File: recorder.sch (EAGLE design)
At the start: 46 parts, among them M1 ELECTRET_MICROPHON-WM-61A, Q1 4.096MHz, T1 MMBT3904 NPN, U1 ISD15100

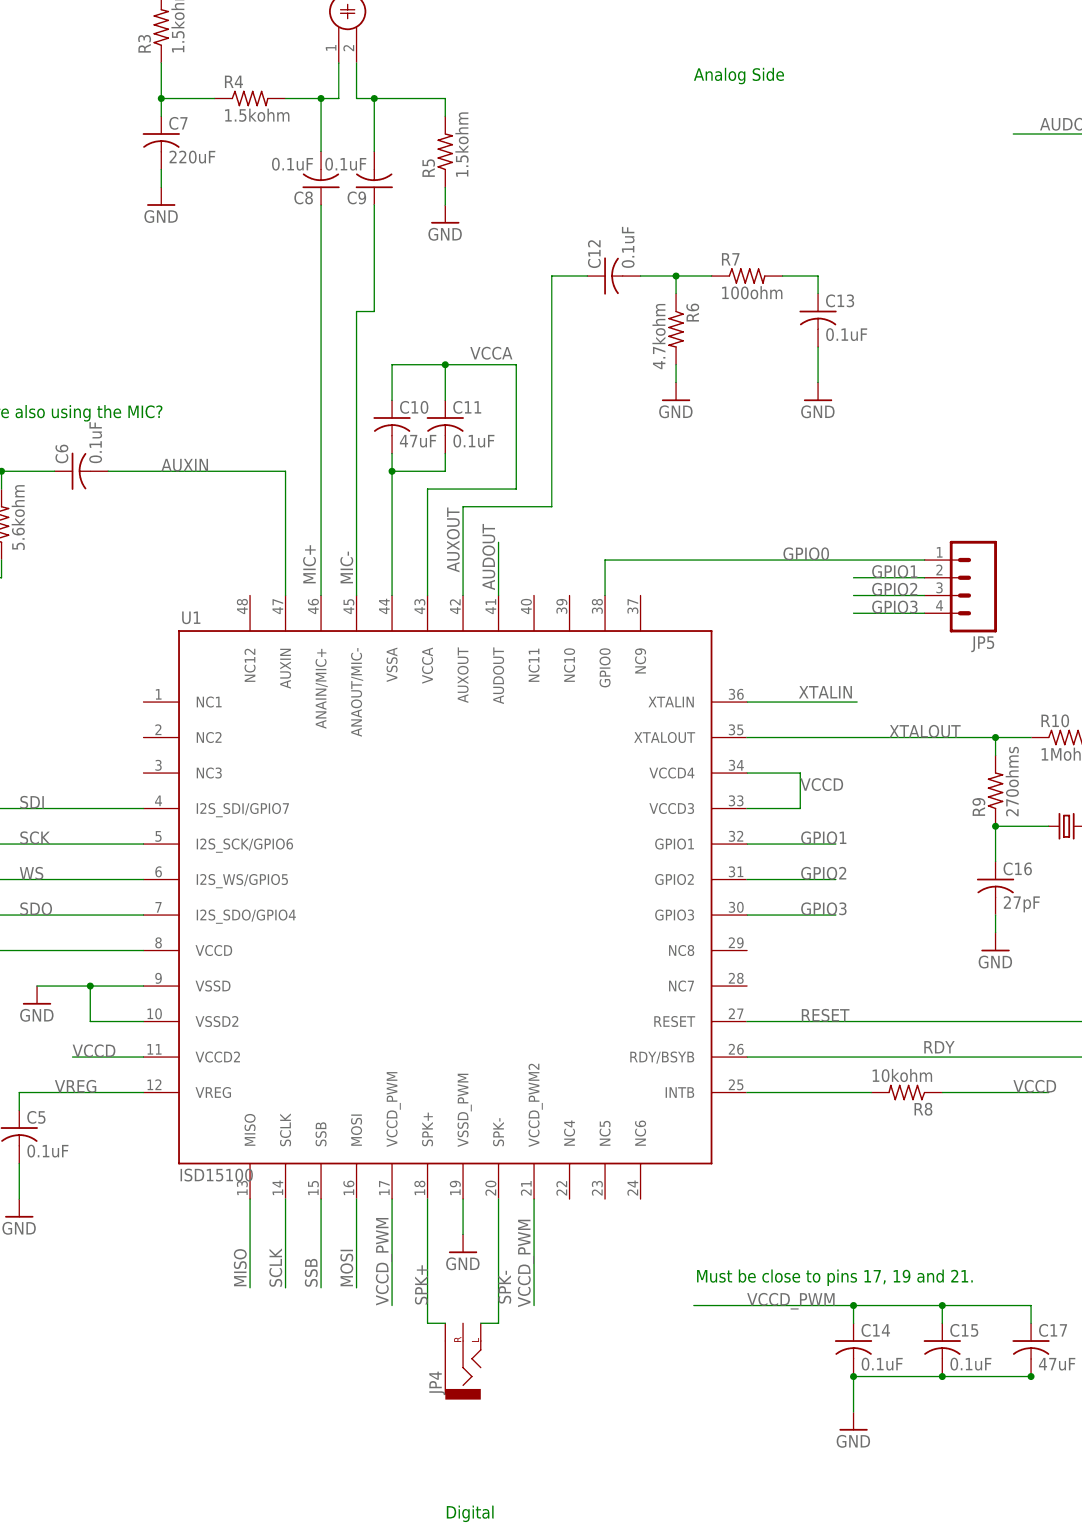
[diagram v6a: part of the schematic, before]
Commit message: upodated BOM. changed mic, headphone jack, and other passive components
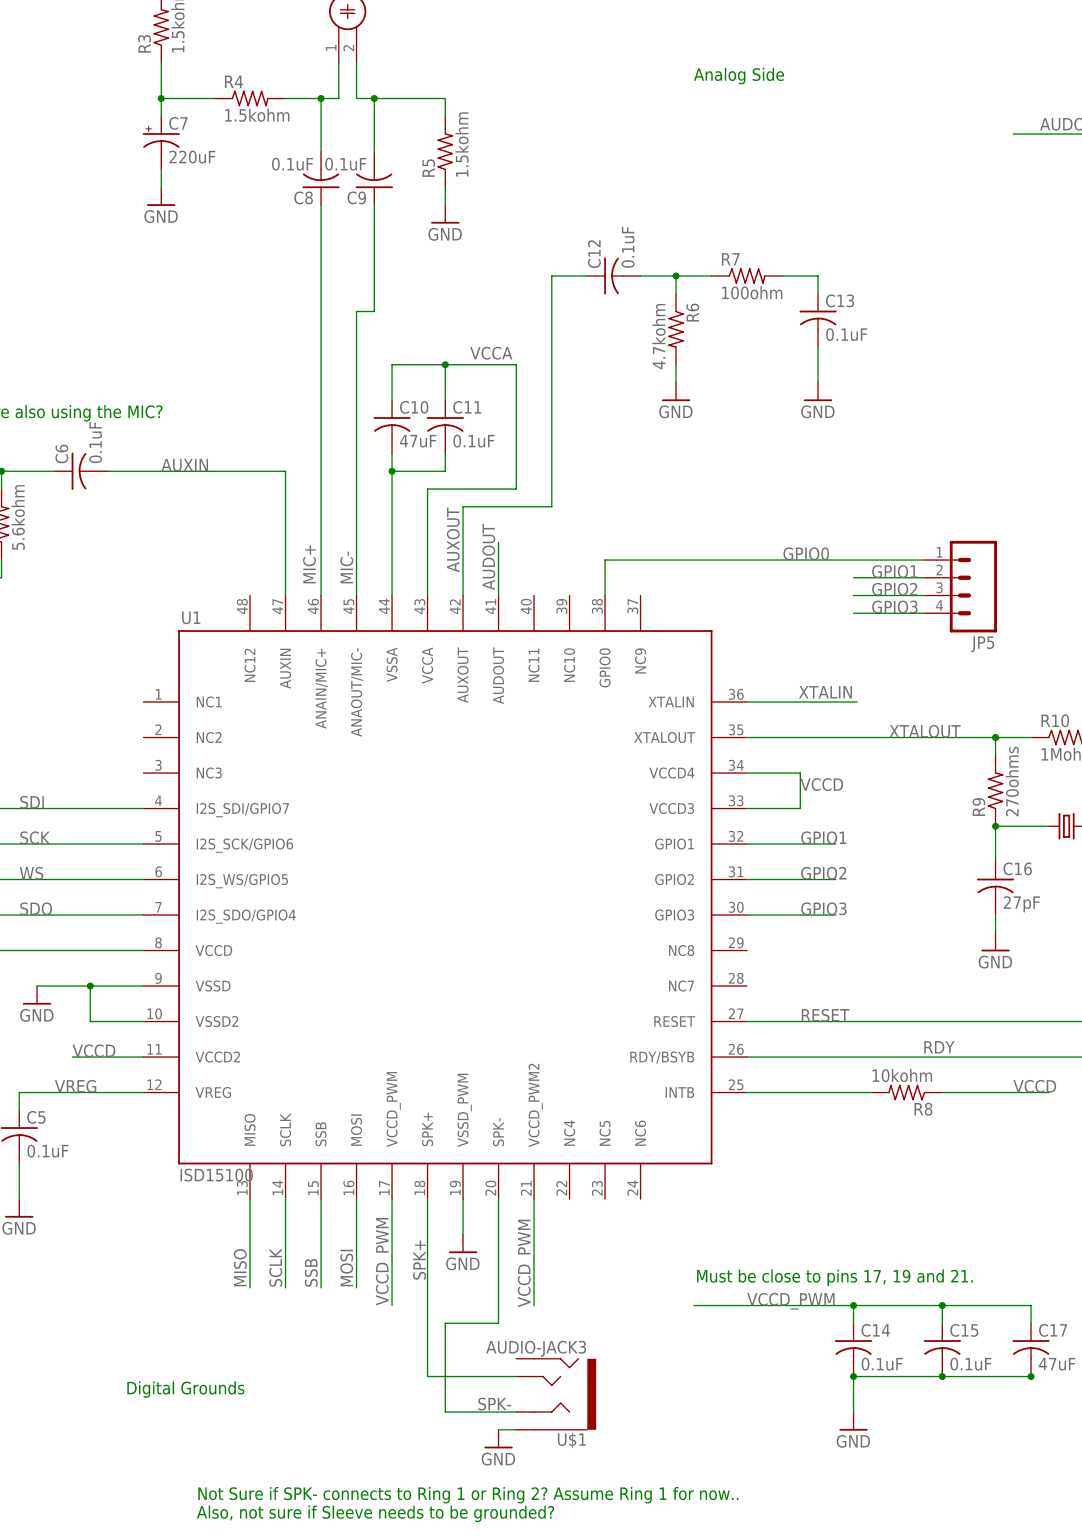
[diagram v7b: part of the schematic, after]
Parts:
- removed JP4: (no value), SparkFun-Connectors:AUDIO-JACKSMD2
- added U$1: AUDIO-JACK3, SparkFun-Connectors:AUDIO-JACK3
- C7: device rcl:C-USC0402 -> rcl:CPOL-US175TMP-0808
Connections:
- net GND: now also C7.-, U$1.EARTH; no longer C7.2
- net N$28: now also C7.+; no longer C7.1
- net SPK+: now also U$1.TIP; no longer JP4.SLEEVE
- net SPK-: now also U$1.RING1; no longer JP4.LEFT
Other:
- note added: "Digital Grounds"
- note added: "Not Sure if SPK- connects to Ring 1 or Ring 2? Assume Ring 1 for now.. Also, not sure if Sleeve needs to be grounded?"
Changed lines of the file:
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@@
 <attribute name="OC_NEWARK" value="81C8514"/>
 </part>
-<part name="C7" library="rcl" deviceset="C-US" device="C0402" value="220uF"/>
 <part name="R3" library="rcl" deviceset="R-US_" device="R0201" value="1.5kohm">
 <attribute name="MF" value="AVX CORPORATION"/>
@@
 <part name="R14" library="rcl" deviceset="R-US_" device="R0402" value="80.6kohm"/>
 <part name="Q1" library="adafruit" deviceset="CRYSTAL" device="SM49" value="4.096MHz"/>
-<part name="JP4" library="SparkFun-Connectors" deviceset="AUDIO-JACK" device="SMD2"/>
 <part name="JP5" library="SparkFun-Connectors" deviceset="M04" device="PTH"/>
 <part name="JP2" library="SparkFun-Connectors" deviceset="M04" device="PTH"/>
@@
 <part name="JP8" library="SparkFun-Connectors" deviceset="M02" device="PTH"/>
 <part name="C1" library="rcl" deviceset="C-US" device="C1206" value="47uF"/>
+<part name="U$1" library="SparkFun-Connectors" deviceset="AUDIO-JACK3" device=""/>
+<part name="GND18" library="SparkFun-Aesthetics" deviceset="GND" device=""/>
+<part name="C7" library="rcl" deviceset="CPOL-US" device="175TMP-0808" value="220uF"/>
 </parts>
 <sheets>
@@
 <text x="106.68" y="223.52" size="1.778" layer="91">Is this redundant if we have a headphone jack? Should speaker be off-board or mounted to PCB?</text>
 <text x="-121.92" y="86.36" size="1.778" layer="91">Digital Side</text>
-<text x="30.48" y="-7.62" size="1.778" layer="91">Digital</text>
+<text x="-15.24" y="10.16" size="1.778" layer="91">Digital Grounds</text>
 <text x="193.04" y="88.9" size="1.778" layer="91">Digital</text>
 <text x="66.04" y="198.12" size="1.778" layer="91">Analog Side</text>
+<text x="-5.08" y="-7.62" size="1.778" layer="91">Not Sure if SPK- connects to Ring 1 or Ring 2? Assume Ring 1 for now..
+Also, not sure if Sleeve needs to be grounded?</text>
 </plain>
 <instances>
@@
 <attribute name="MPN" x="2.54" y="195.58" size="1.778" layer="96" rot="R90" display="off"/>
 </instance>
-<instance part="C7" gate="G$1" x="-10.16" y="190.5"/>
 <instance part="R3" gate="G$1" x="-10.16" y="205.74" rot="R90">
 <attribute name="OC_NEWARK" x="-10.16" y="205.74" size="1.778" layer="96" rot="R180" display="off"/>
@@
 <instance part="R14" gate="G$1" x="149.86" y="81.28" rot="R270"/>
 <instance part="Q1" gate="G$1" x="119.38" y="91.44"/>
-<instance part="JP4" gate="G$1" x="33.02" y="15.24" rot="R90"/>
 <instance part="JP5" gate="G$1" x="104.14" y="127" rot="R180"/>
 <instance part="JP2" gate="G$1" x="-68.58" y="12.7"/>
@@
 <instance part="JP8" gate="G$1" x="-91.44" y="71.12"/>
 <instance part="C1" gate="G$1" x="-66.04" y="68.58"/>
+<instance part="U$1" gate="G$1" x="45.72" y="10.16" rot="R180"/>
+<instance part="GND18" gate="1" x="38.1" y="2.54"/>
+<instance part="C7" gate="G$1" x="-10.16" y="190.5"/>
 </instances>
 <busses>
@@
 <segment>
 <pinref part="U1" gate="G$1" pin="SPK+"/>
-<wire x1="27.94" y1="20.32" x2="27.94" y2="38.1" width="0.1524" layer="91"/>
-<wire x1="30.48" y1="20.32" x2="27.94" y2="20.32" width="0.1524" layer="91"/>
-<pinref part="JP4" gate="G$1" pin="SLEEVE"/>
-<label x="27.94" y="22.86" size="1.778" layer="95" rot="R90"/>
+<wire x1="27.94" y1="12.7" x2="27.94" y2="38.1" width="0.1524" layer="91"/>
+<label x="27.686" y="26.416" size="1.778" layer="95" rot="R90"/>
+<pinref part="U$1" gate="G$1" pin="TIP"/>
+<wire x1="27.94" y1="12.7" x2="40.64" y2="12.7" width="0.1524" layer="91"/>
 </segment>
 </net>
@@
 <pinref part="U1" gate="G$1" pin="SPK-"/>
 <wire x1="38.1" y1="20.32" x2="38.1" y2="38.1" width="0.1524" layer="91"/>
-<wire x1="35.56" y1="20.32" x2="38.1" y2="20.32" width="0.1524" layer="91"/>
-<pinref part="JP4" gate="G$1" pin="LEFT"/>
-<label x="38.1" y="27.94" size="1.778" layer="95" rot="R270"/>
+<label x="35.052" y="7.874" size="1.778" layer="95"/>
+<wire x1="38.1" y1="20.32" x2="30.48" y2="20.32" width="0.1524" layer="91"/>
+<wire x1="30.48" y1="20.32" x2="30.48" y2="7.62" width="0.1524" layer="91"/>
+<pinref part="U$1" gate="G$1" pin="RING1"/>
+<wire x1="30.48" y1="7.62" x2="40.64" y2="7.62" width="0.1524" layer="91"/>
 </segment>
 </net>
@@
 <net name="N$28" class="0">
 <segment>
-<pinref part="C7" gate="G$1" pin="1"/>
 <pinref part="R3" gate="G$1" pin="1"/>
 <wire x1="-10.16" y1="193.04" x2="-10.16" y2="195.58" width="0.1524" layer="91"/>
@@
 <wire x1="-2.54" y1="195.58" x2="-10.16" y2="195.58" width="0.1524" layer="91"/>
 <junction x="-10.16" y="195.58"/>
+<pinref part="C7" gate="G$1" pin="+"/>
 </segment>
 </net>
@@
 </segment>
 <segment>
-<pinref part="C7" gate="G$1" pin="2"/>
 <wire x1="-10.16" y1="182.88" x2="-10.16" y2="185.42" width="0.1524" layer="91"/>
 <pinref part="GND2" gate="1" pin="GND"/>
+<pinref part="C7" gate="G$1" pin="-"/>
 </segment>
 <segment>
@@
 <wire x1="-78.74" y1="71.12" x2="-78.74" y2="66.04" width="0.1524" layer="91"/>
 </segment>
+<segment>
+<pinref part="GND18" gate="1" pin="GND"/>
+<pinref part="U$1" gate="G$1" pin="EARTH"/>
+<wire x1="38.1" y1="5.08" x2="40.64" y2="5.08" width="0.1524" layer="91"/>
+</segment>
 </net>
 </nets>
@@
 </schematic>
 </drawing>
+<compatibility>
+<note version="6.3" minversion="6.2.2" severity="warning">
+Since Version 6.2.2 text objects can contain more than one line,
+which will not be processed correctly with this version.
+</note>
+</compatibility>
 </eagle>

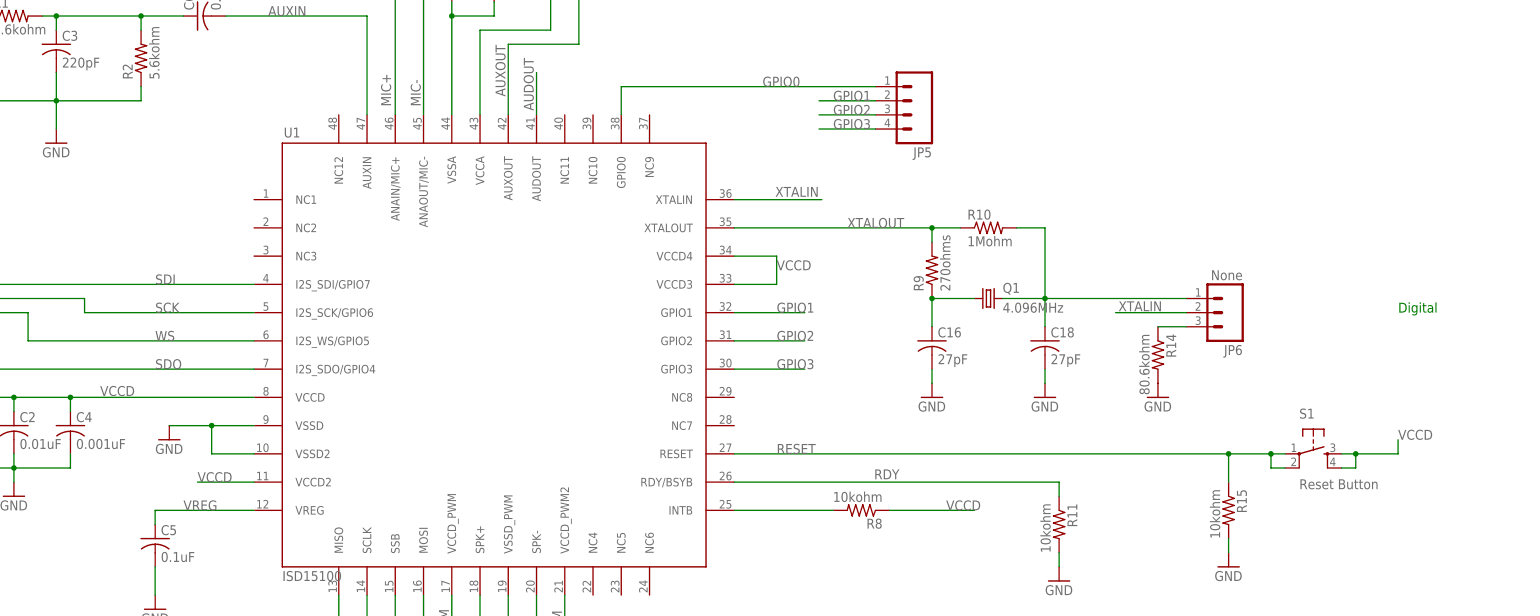
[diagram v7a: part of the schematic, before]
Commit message: moved gnd plane to bottom layer, added vias to gnd, and adjust components around to pass DRC
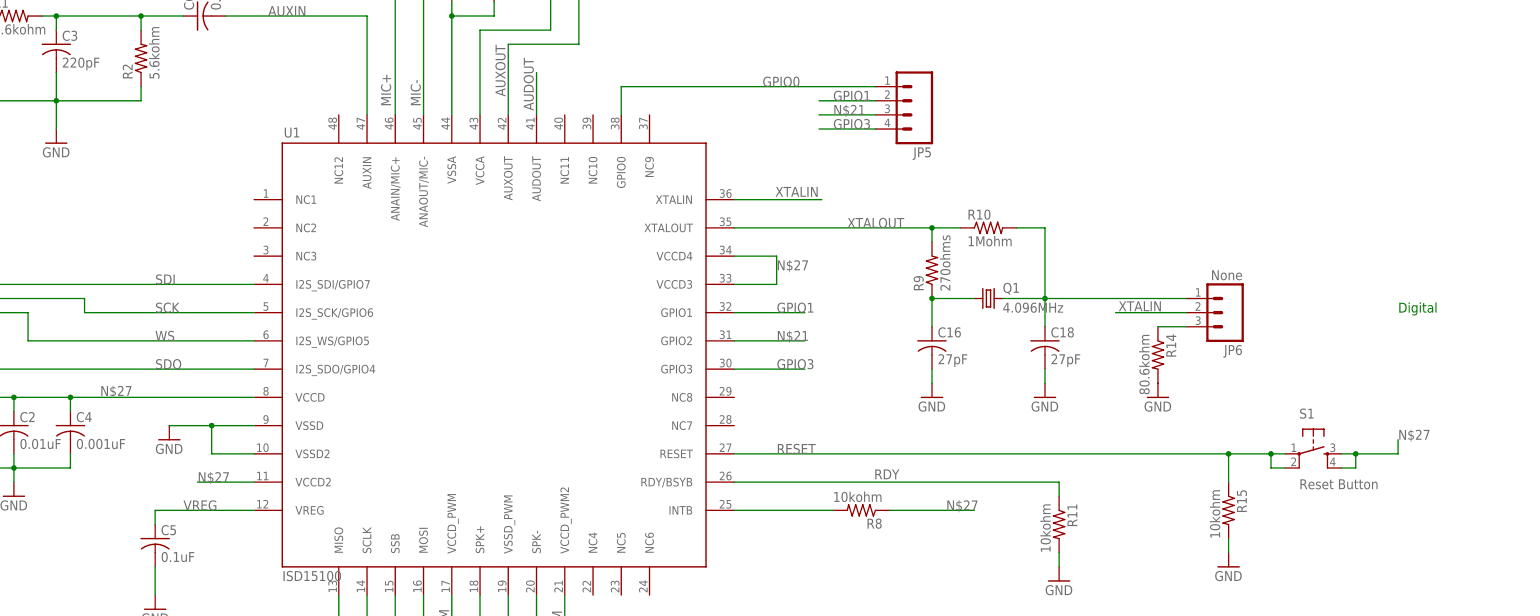
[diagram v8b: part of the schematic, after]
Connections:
- net GPIO2 renamed N$21
- net VCCD renamed N$27
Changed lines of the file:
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@@
 </segment>
 </net>
-<net name="VCCD" class="0">
+<net name="N$27" class="0">
 <segment>
 <pinref part="U1" gate="G$1" pin="VCCD4"/>
@@
 </segment>
 </net>
-<net name="GPIO2" class="0">
+<net name="N$21" class="0">
 <segment>
 <pinref part="U1" gate="G$1" pin="GPIO2"/>
